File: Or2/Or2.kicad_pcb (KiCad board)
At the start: 2 copper layers, 31.8 x 28 mm, 13 parts, among them J1 In1, J2 In2, J3 Out, J4 Thru1, J5 Thru2, U1 Or2_SN74AHC1G32

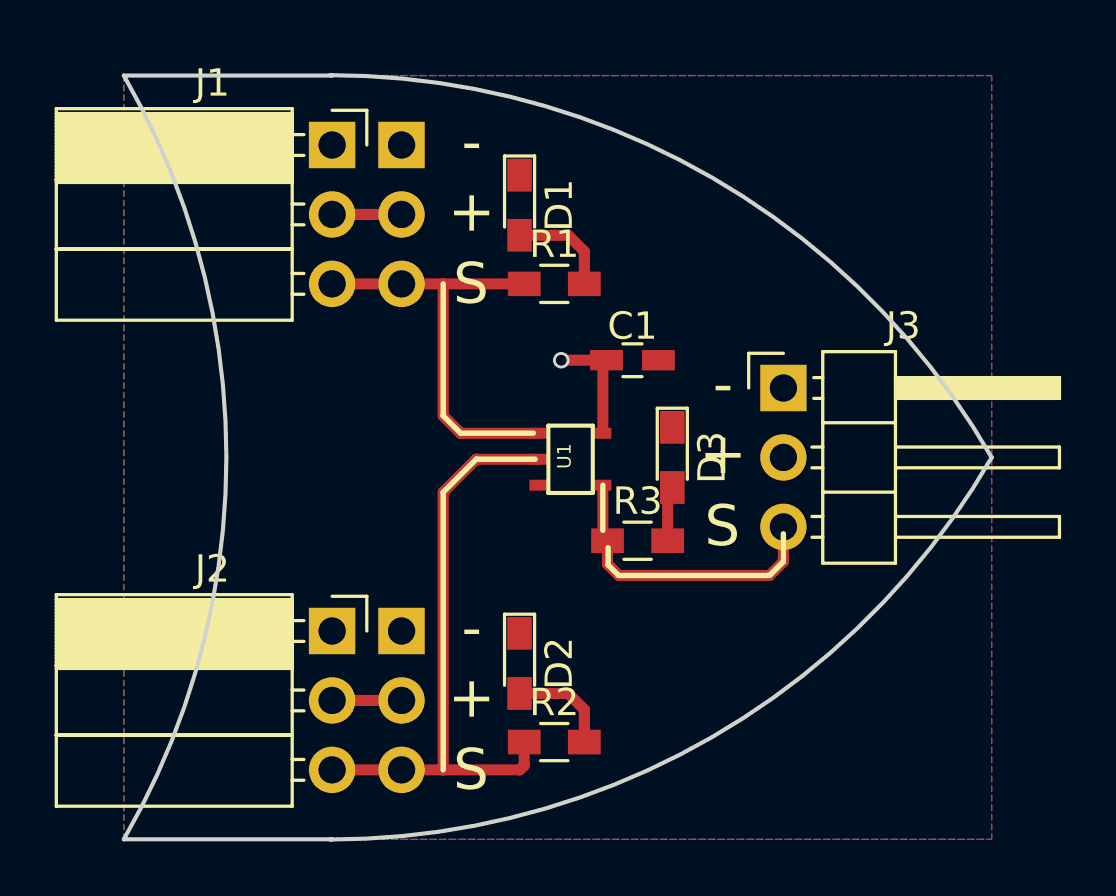
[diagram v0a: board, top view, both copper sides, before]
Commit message: Made XOR Board and modified FA
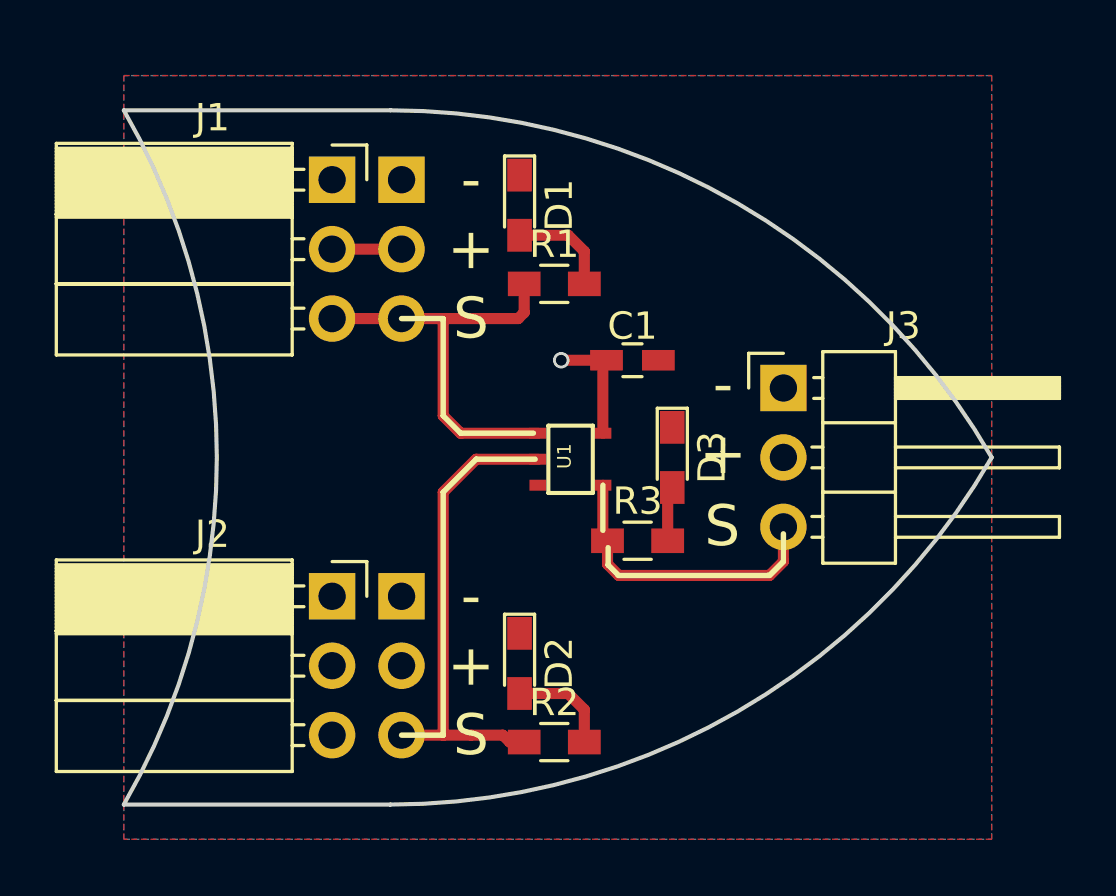
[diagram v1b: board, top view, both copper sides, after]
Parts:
- moved J1 1.27 mm to (139.7, 80.0)
- moved J4 1.27 mm to (142.2, 80.0)
- moved J2 1.27 mm to (139.7, 95.2)
- moved J5 1.27 mm to (142.2, 95.2)
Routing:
- net /In2: track 22.1 -> 17.4 mm
- net Vin: track 9.46 -> 6.92 mm
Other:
- board size 31.8 x 28 mm -> 31.7 x 25.4 mm
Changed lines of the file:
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@@
   (general
     (links 26)
-    (no_connects 0)
-    (area 104.01115 48.13115 190.600001 132.180001)
+    (no_connects 1)
+    (area 110.008599 77.39472 163.905001 102.94528)
     (thickness 1.6)
     (drawings 30)
-    (tracks 35)
+    (tracks 37)
     (zones 0)
     (modules 13)
@@
     (47 F.CrtYd user)
     (48 B.Fab user)
-    (49 F.Fab user hide)
+    (49 F.Fab user)
   )
   (setup
@@
   )
   (module Socket_Strips:Socket_Strip_Angled_1x03_Pitch2.54mm (layer F.Cu)
-    (at 139.7 78.74)
+    (at 139.7 80.01)
     (descr "Through hole angled socket strip, 1x03, 2.54mm pitch, 8.51mm socket length, single row")
     (tags "Through hole angled socket strip THT 1x03 2.54mm single row")
@@
   )
   (module Socket_Strips:Socket_Strip_Angled_1x03_Pitch2.54mm (layer F.Cu)
-    (at 139.7 96.52)
+    (at 139.7 95.25)
     (descr "Through hole angled socket strip, 1x03, 2.54mm pitch, 8.51mm socket length, single row")
     (tags "Through hole angled socket strip THT 1x03 2.54mm single row")
@@
   )
   (module Pin_Headers:Pin_Header_Angled_1x03_Pitch2.54mm (layer B.Cu)
-    (at 142.24 78.74 180)
+    (at 142.24 80.01 180)
     (descr "Through hole angled pin header, 1x03, 2.54mm pitch, 6mm pin length, single row")
     (tags "Through hole angled pin header THT 1x03 2.54mm single row")
@@
   )
   (module Pin_Headers:Pin_Header_Angled_1x03_Pitch2.54mm (layer B.Cu)
-    (at 142.24 96.52 180)
+    (at 142.24 95.25 180)
     (descr "Through hole angled pin header, 1x03, 2.54mm pitch, 6mm pin length, single row")
     (tags "Through hole angled pin header THT 1x03 2.54mm single row")
@@
       (net 8 /Out))
   )
+  (gr_line (start 132.08 102.87) (end 141.83 102.87) (layer Edge.Cuts) (width 0.15))
+  (gr_line (start 141.83 77.47) (end 132.08 77.47) (layer Edge.Cuts) (width 0.15))
+  (gr_arc (start 141.833116 77.469721) (end 141.833116 102.869721) (angle -59.99927222) (layer Edge.Cuts) (width 0.15))
+  (gr_arc (start 141.833116 102.870279) (end 141.833116 77.470279) (angle 59.99927222) (layer Edge.Cuts) (width 0.15))
+  (gr_arc (start 110.0836 90.17) (end 132.08 77.47) (angle 60.00145556) (layer Edge.Cuts) (width 0.15))
+  (dimension 31.75 (width 0.3) (layer F.Fab)
+    (gr_text "1.2500 in" (at 147.955 114.38) (layer F.Fab)
+      (effects (font (size 1.5 1.5) (thickness 0.3)))
+    )
+    (feature1 (pts (xy 163.83 104.14) (xy 163.83 115.73)))
+    (feature2 (pts (xy 132.08 104.14) (xy 132.08 115.73)))
+    (crossbar (pts (xy 132.08 113.03) (xy 163.83 113.03)))
+    (arrow1a (pts (xy 163.83 113.03) (xy 162.703496 113.616421)))
+    (arrow1b (pts (xy 163.83 113.03) (xy 162.703496 112.443579)))
+    (arrow2a (pts (xy 132.08 113.03) (xy 133.206504 113.616421)))
+    (arrow2b (pts (xy 132.08 113.03) (xy 133.206504 112.443579)))
+  )
+  (gr_line (start 143.764 85.09) (end 142.24 85.09) (layer F.SilkS) (width 0.2))
+  (gr_line (start 143.764 100.33) (end 142.24 100.33) (layer F.SilkS) (width 0.2))
+  (gr_line (start 143.764 91.44) (end 143.764 100.33) (layer F.SilkS) (width 0.2))
+  (gr_line (start 143.764 85.09) (end 143.764 88.646) (layer F.SilkS) (width 0.2))
   (gr_line (start 156.21 93.98) (end 156.21 92.964) (layer F.SilkS) (width 0.2))
   (gr_line (start 155.702 94.488) (end 156.21 93.98) (layer F.SilkS) (width 0.2))
@@
   (gr_line (start 144.9705 90.2335) (end 143.764 91.44) (layer F.SilkS) (width 0.2))
   (gr_line (start 147.1295 90.2335) (end 144.9705 90.2335) (layer F.SilkS) (width 0.2))
-  (gr_line (start 143.764 101.6) (end 143.764 91.44) (layer F.SilkS) (width 0.2))
-  (gr_line (start 143.764 88.646) (end 143.764 83.82) (layer F.SilkS) (width 0.2))
   (gr_line (start 144.399 89.281) (end 143.764 88.646) (layer F.SilkS) (width 0.2))
   (gr_line (start 147.066 89.281) (end 144.399 89.281) (layer F.SilkS) (width 0.2))
@@
     (effects (font (size 1.5 1.5) (thickness 0.3)))
   )
-  (gr_text S (at 144.78 101.6) (layer F.SilkS)
+  (gr_text S (at 144.78 100.33) (layer F.SilkS)
     (effects (font (size 1.5 1.5) (thickness 0.3)))
   )
-  (gr_text - (at 144.8054 96.4184) (layer F.SilkS)
+  (gr_text - (at 144.78 95.25) (layer F.SilkS)
     (effects (font (size 1.5 1.5) (thickness 0.3)))
   )
-  (gr_text + (at 144.8054 98.9584) (layer F.SilkS)
+  (gr_text + (at 144.78 97.79) (layer F.SilkS)
     (effects (font (size 1.5 1.5) (thickness 0.3)))
   )
-  (gr_text S (at 144.78 83.82) (layer F.SilkS)
+  (gr_text S (at 144.78 85.09) (layer F.SilkS)
     (effects (font (size 1.5 1.5) (thickness 0.3)))
   )
-  (gr_text + (at 144.8054 81.1784) (layer F.SilkS)
+  (gr_text + (at 144.78 82.55) (layer F.SilkS)
     (effects (font (size 1.5 1.5) (thickness 0.3)))
   )
-  (gr_text - (at 144.8054 78.6384) (layer F.SilkS)
+  (gr_text - (at 144.78 80.01) (layer F.SilkS)
     (effects (font (size 1.5 1.5) (thickness 0.3)))
   )
-  (gr_arc (start 107.95 90.17) (end 132.08 76.2) (angle 60.13716564) (layer Edge.Cuts) (width 0.15))
-  (gr_circle (center 132.08 76.2) (end 133.35 104.14) (layer F.Fab) (width 0.2))
-  (gr_circle (center 132.08 104.14) (end 132.08 76.2) (layer F.Fab) (width 0.2))
-  (gr_line (start 132.08 76.2) (end 139.7 76.2) (layer Edge.Cuts) (width 0.15))
-  (gr_line (start 132.08 104.14) (end 139.7 104.14) (layer Edge.Cuts) (width 0.15))
-  (gr_arc (start 139.6238 76.2) (end 163.83 90.17) (angle 60.00968681) (layer Edge.Cuts) (width 0.15))
-  (gr_arc (start 139.624552 104.124923) (end 139.624552 76.184923) (angle 60.03569462) (layer Edge.Cuts) (width 0.15))
-  (gr_line (start 132.08 90.17) (end 190.5 90.17) (layer F.Fab) (width 0.2))
+  (segment (start 139.7 82.55) (end 142.24 82.55) (width 0.4064) (layer F.Cu) (net 1))
   (segment (start 149.738 86.614) (end 148.082 86.614) (width 0.4064) (layer F.Cu) (net 1))
   (via (at 148.082 86.614) (size 0.6) (drill 0.4) (layers F.Cu B.Cu) (net 1))
   (segment (start 149.606 89.286) (end 149.606 86.746) (width 0.4064) (layer F.Cu) (net 1))
   (segment (start 149.606 86.746) (end 149.738 86.614) (width 0.4064) (layer F.Cu) (net 1))
-  (segment (start 139.7 99.06) (end 142.24 99.06) (width 0.4064) (layer F.Cu) (net 1))
-  (segment (start 139.7 81.28) (end 142.24 81.28) (width 0.4064) (layer F.Cu) (net 1))
   (segment (start 148.336 82.042) (end 148.928 82.634) (width 0.4064) (layer F.Cu) (net 3))
   (segment (start 148.928 82.634) (end 148.928 83.82) (width 0.4064) (layer F.Cu) (net 3))
@@
   (segment (start 151.976 93.218) (end 151.976 91.44) (width 0.4064) (layer F.Cu) (net 5))
   (segment (start 151.976 91.44) (end 152.146 91.27) (width 0.4064) (layer F.Cu) (net 5))
+  (segment (start 146.5072 85.09) (end 146.728 84.8692) (width 0.4064) (layer F.Cu) (net 6))
+  (segment (start 146.728 84.8692) (end 146.728 83.82) (width 0.4064) (layer F.Cu) (net 6))
+  (segment (start 143.7132 85.09) (end 146.5072 85.09) (width 0.4064) (layer F.Cu) (net 6))
+  (segment (start 143.764 85.1408) (end 143.764 88.646) (width 0.4064) (layer F.Cu) (net 6))
+  (segment (start 142.24 85.09) (end 143.7132 85.09) (width 0.4064) (layer F.Cu) (net 6))
+  (segment (start 143.7132 85.09) (end 143.764 85.1408) (width 0.4064) (layer F.Cu) (net 6))
+  (segment (start 139.7 85.09) (end 142.24 85.09) (width 0.4064) (layer F.Cu) (net 6))
   (segment (start 143.764 88.646) (end 144.404 89.286) (width 0.4064) (layer F.Cu) (net 6))
   (segment (start 144.404 89.286) (end 147.231 89.286) (width 0.4064) (layer F.Cu) (net 6))
-  (segment (start 143.764 83.82) (end 146.728 83.82) (width 0.4064) (layer F.Cu) (net 6))
-  (segment (start 143.764 83.82) (end 143.764 88.646) (width 0.4064) (layer F.Cu) (net 6))
-  (segment (start 142.24 83.82) (end 143.764 83.82) (width 0.4064) (layer F.Cu) (net 6))
-  (segment (start 139.7 83.82) (end 142.24 83.82) (width 0.4064) (layer F.Cu) (net 6))
+  (segment (start 146.728 100.584) (end 146.2024 100.584) (width 0.4064) (layer F.Cu) (net 7))
+  (segment (start 146.2024 100.584) (end 145.9484 100.33) (width 0.4064) (layer F.Cu) (net 7))
+  (segment (start 145.9484 100.33) (end 144.78 100.33) (width 0.4064) (layer F.Cu) (net 7))
+  (segment (start 144.78 100.33) (end 143.764 100.33) (width 0.4064) (layer F.Cu) (net 7))
+  (segment (start 142.24 100.33) (end 143.764 100.33) (width 0.4064) (layer F.Cu) (net 7))
+  (segment (start 143.764 100.33) (end 143.764 91.44) (width 0.4064) (layer F.Cu) (net 7))
   (segment (start 143.764 91.44) (end 144.968 90.236) (width 0.4064) (layer F.Cu) (net 7))
   (segment (start 144.968 90.236) (end 147.231 90.236) (width 0.4064) (layer F.Cu) (net 7))
-  (segment (start 143.764 101.6) (end 146.5684 101.6) (width 0.4064) (layer F.Cu) (net 7))
-  (segment (start 143.764 101.6) (end 143.764 91.44) (width 0.4064) (layer F.Cu) (net 7))
-  (segment (start 142.24 101.6) (end 143.764 101.6) (width 0.4064) (layer F.Cu) (net 7))
-  (segment (start 146.5684 101.6) (end 146.728 101.4404) (width 0.4064) (layer F.Cu) (net 7))
-  (segment (start 146.728 101.4404) (end 146.728 100.584) (width 0.4064) (layer F.Cu) (net 7))
-  (segment (start 139.7 101.6) (end 142.24 101.6) (width 0.4064) (layer F.Cu) (net 7))
   (segment (start 149.776 93.218) (end 149.776 94.0744) (width 0.4064) (layer F.Cu) (net 8))
   (segment (start 149.776 94.0744) (end 150.1896 94.488) (width 0.4064) (layer F.Cu) (net 8))
